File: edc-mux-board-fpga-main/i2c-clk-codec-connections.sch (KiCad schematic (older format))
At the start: 72 parts, among them U57 CDCLVC1108, U58 CDCLVC1108, U59 TCA9555RTWR, U60 TCA9548A, U61 TCA9548A

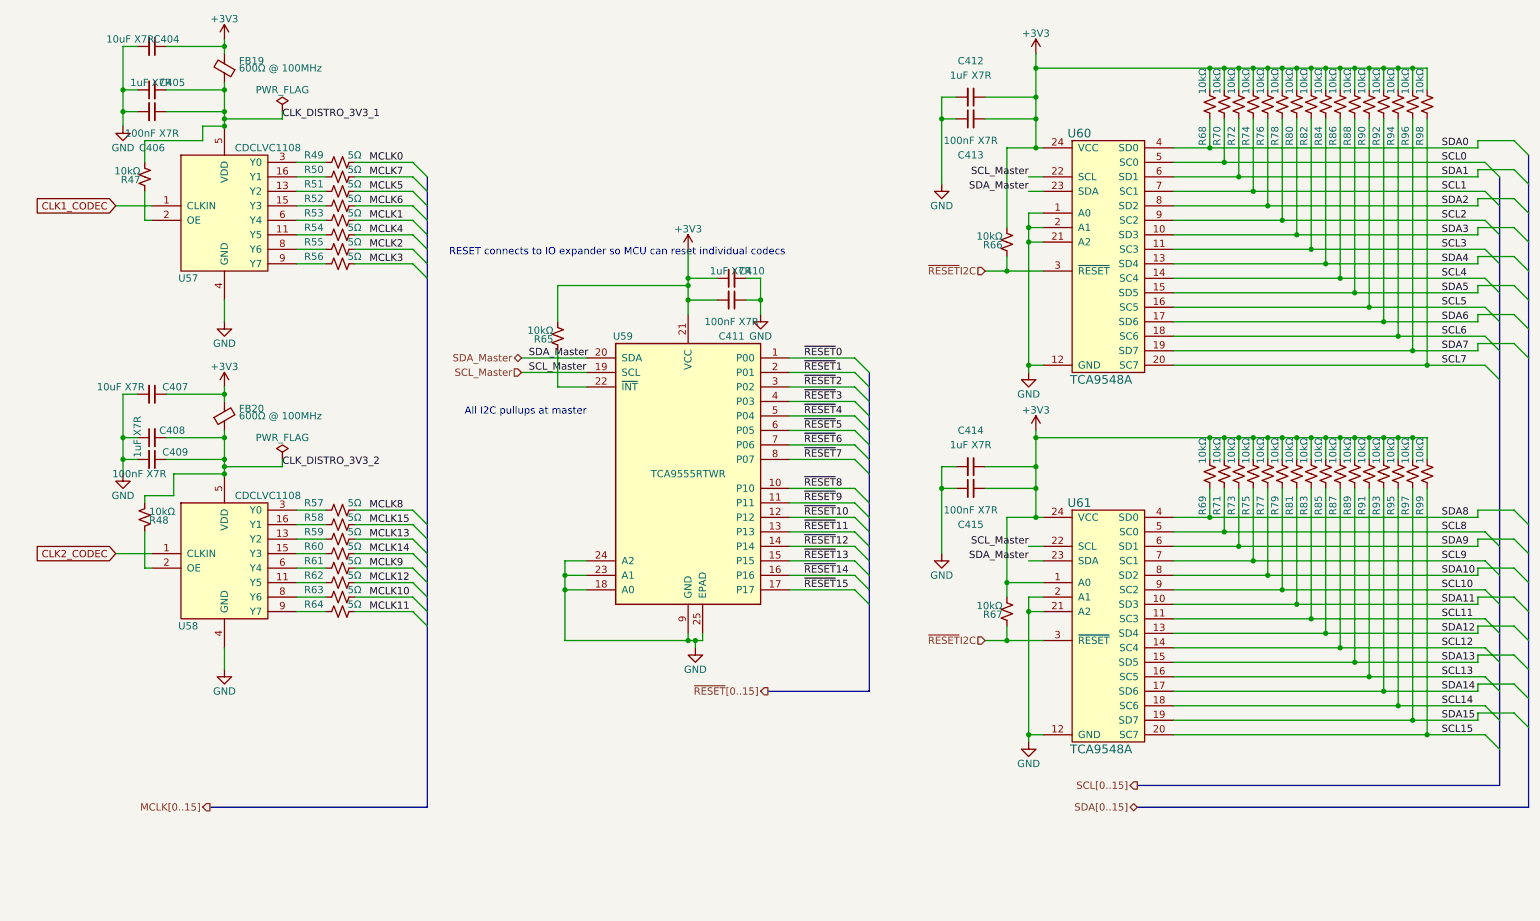
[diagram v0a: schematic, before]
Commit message: removed 8 codecs and support circuitry
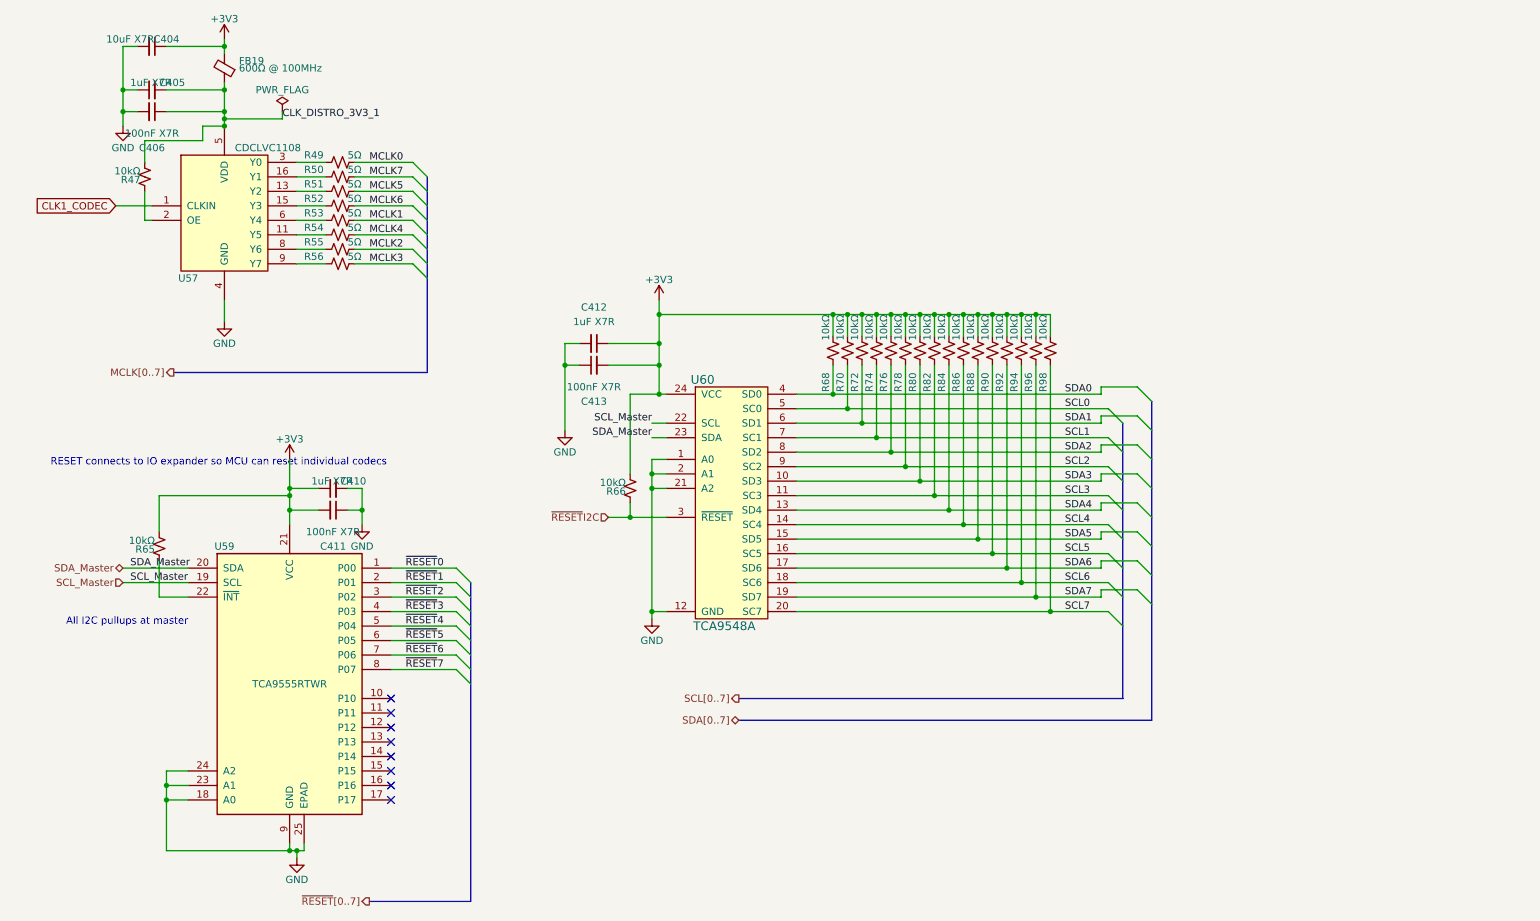
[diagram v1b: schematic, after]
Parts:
- removed C407: 10uF X7R, Capacitor_SMD:C_1206_3216Metric, symbol Device:C_Small
- removed C408, C414: 1uF X7R, Capacitor_SMD:C_0603_1608Metric, symbol Device:C_Small
- removed C409, C415: 100nF X7R, Capacitor_SMD:C_0603_1608Metric, symbol Device:C_Small
- removed FB20: 600Ω @ 100MHz, Inductor_SMD:L_0805_2012Metric, symbol Device:Ferrite_Bead_Small
- removed R48, R67, R69, R71, R73, R75, R77, R79, R81, R83, R85, R87, R89, R91, R93, R95, R97, R99: 10kΩ, Resistor_SMD:R_0402_1005Metric, symbol Device:R_Small_US
- removed R57, R58, R59, R60, R61, R62, R63, R64: 5Ω, Resistor_SMD:R_0402_1005Metric, symbol Device:R_Small_US
- removed U58: CDCLVC1108, Package_SO:TSSOP-16_4.4x5mm_P0.65mm, symbol SW-Texas:CDCLVC1108
- removed U61: TCA9548A, Package_SO:TSSOP-24_4.4x7.8mm_P0.65mm, symbol SW-Texas:TCA9548A
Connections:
- net ~RESET~10: no longer names the net of U59.12 (P12)
- net ~RESET~11: no longer names the net of U59.13 (P13)
- net ~RESET~12: no longer names the net of U59.14 (P14)
- net ~RESET~13: no longer names the net of U59.15 (P15)
- net ~RESET~14: no longer names the net of U59.16 (P16)
- net ~RESET~15: no longer names the net of U59.17 (P17)
- net ~RESET~8: no longer names the net of U59.10 (P10)
- net ~RESET~9: no longer names the net of U59.11 (P11)
- no-connect marks 0 -> 8
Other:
- moved on the sheet: C410, C411, C412, C413, R65, R66, R68, R70, R72, R74, R76, R78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

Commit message: Reannotate main schematic and pcb after expansion transition
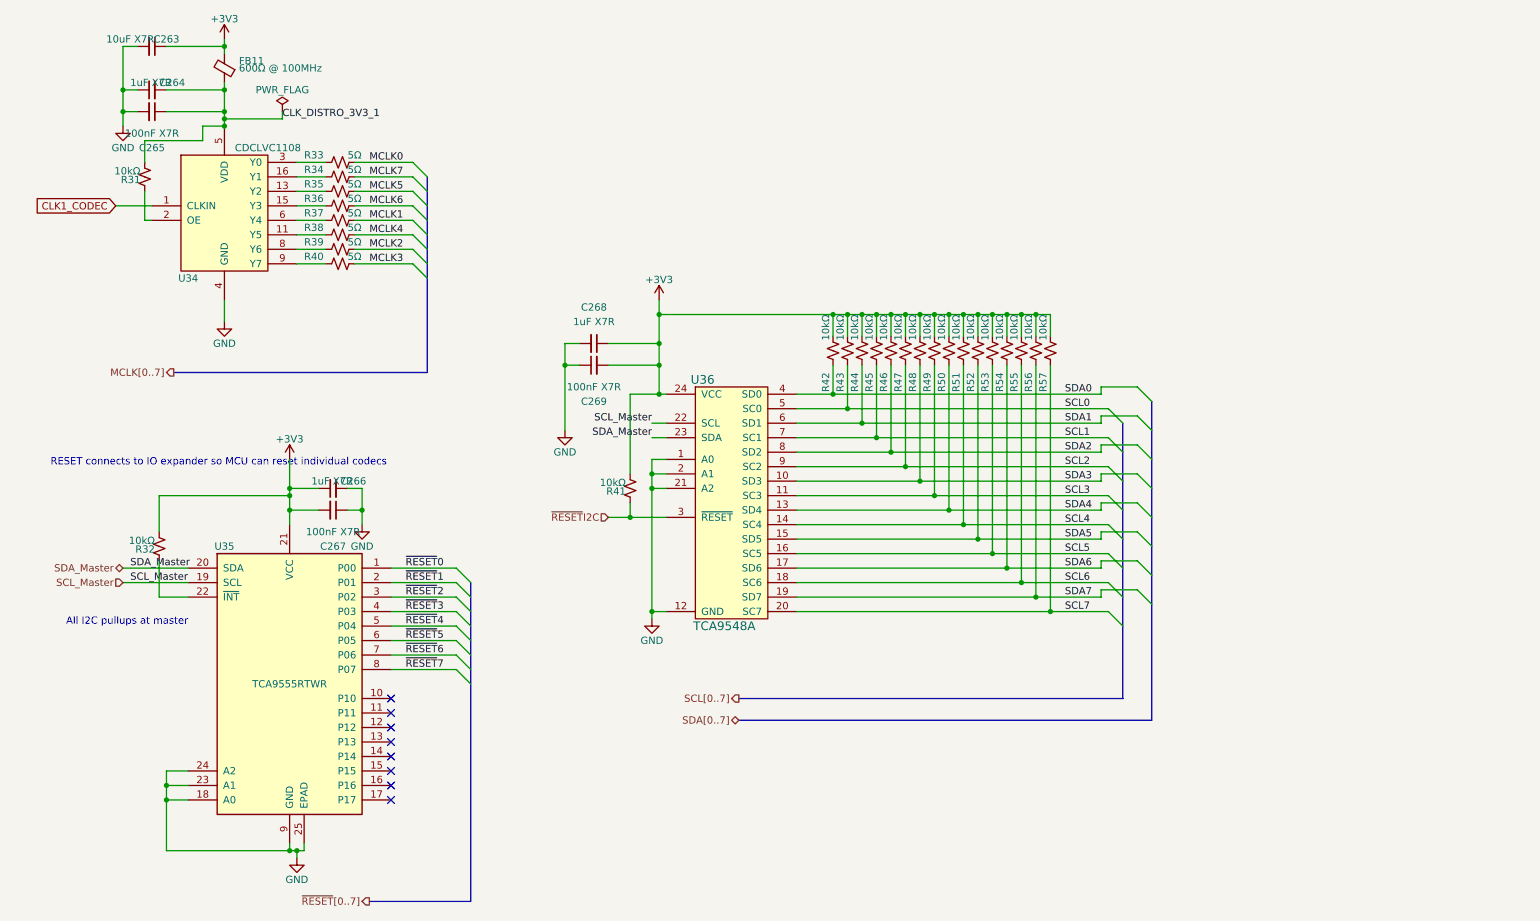
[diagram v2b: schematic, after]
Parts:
- renumbered C404 to C263, C405 to C264, C406 to C265, C410 to C266, C411 to C267, C412 to C268, C413 to C269, FB19 to FB11, R47 to R31, R65 to R32, R49 to R33, R50 to R34, R51 to R35, R52 to R36, R53 to R37, R54 to R38, R55 to R39, R56 to R40, R66 to R41, R68 to R42, R70 to R43, R72 to R44, R74 to R45, R76 to R46, R78 to R47, R80 to R48, R82 to R49, R84 to R50, R86 to R51, R88 to R52, R90 to R53, R92 to R54, R94 to R55, R96 to R56, R98 to R57, U57 to U34, U59 to U35, U60 to U36

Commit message: swapping 100nF capacitors from 0603 to 0402 size
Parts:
- C265, C267, C269: footprint Capacitor_SMD:C_0603_1608Metric -> Capacitor_SMD:C_0402_1005Metric; Characteristics CAP CER 0.1UF 25V X7R 0603 -> CAP CER 0.1UF 25V X7R 0402; Manufacturer Kemet -> AVX; Manufacturers Part Number C0603C104J3RACAUTO -> 04023C104JAT2A; Package ID 0603in/1608mm -> 0402in/1005mm
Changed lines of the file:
@@
 F 0 "C265" V 1200 1350 50  0000 C CNN
 F 1 "100nF X7R" V 1300 1350 50  0000 C CNN
-F 2 "Capacitor_SMD:C_0603_1608Metric" H 1450 1350 50  0001 C CNN
-F 3 "https://content.kemet.com/datasheets/KEM_C1023_X7R_AUTO_SMD.pdf" H 1450 1350 50  0001 C CNN
-F 4 "0603in/1608mm" H -6000 -2400 50  0001 C CNN "Package ID"
-F 5 "Kemet" H 0   0   50  0001 C CNN "Manufacturer"
-F 6 "C0603C104J3RACAUTO" H 0   0   50  0001 C CNN "Manufacturers Part Number"
-F 7 "CAP CER 0.1UF 25V X7R 0603" H 0   0   50  0001 C CNN "Characteristics"
+F 2 "Capacitor_SMD:C_0402_1005Metric" H 1450 1350 50  0001 C CNN
+F 3 "http://datasheets.avx.com/X7RDielectric.pdf" H 1450 1350 50  0001 C CNN
+F 4 "0402in/1005mm" H -6000 -2400 50  0001 C CNN "Package ID"
+F 5 "AVX" H 0   0   50  0001 C CNN "Manufacturer"
+F 6 "04023C104JAT2A" H 0   0   50  0001 C CNN "Manufacturers Part Number"
+F 7 "CAP CER 0.1UF 25V X7R 0402" H 0   0   50  0001 C CNN "Characteristics"
 F 8 "MLCC Capacitor" H 0   0   50  0001 C CNN "Description"
 	1    1450 1350
@@
 F 0 "C267" V 2450 4100 50  0000 C CNN
 F 1 "100nF X7R" V 2550 4100 50  0000 C CNN
-F 2 "Capacitor_SMD:C_0603_1608Metric" H 2700 4100 50  0001 C CNN
-F 3 "https://content.kemet.com/datasheets/KEM_C1023_X7R_AUTO_SMD.pdf" H 2700 4100 50  0001 C CNN
-F 4 "0603in/1608mm" H -4750 350 50  0001 C CNN "Package ID"
-F 5 "Kemet" H -2750 1450 50  0001 C CNN "Manufacturer"
-F 6 "C0603C104J3RACAUTO" H -2750 1450 50  0001 C CNN "Manufacturers Part Number"
-F 7 "CAP CER 0.1UF 25V X7R 0603" H -2750 1450 50  0001 C CNN "Characteristics"
+F 2 "Capacitor_SMD:C_0402_1005Metric" H 2700 4100 50  0001 C CNN
+F 3 "http://datasheets.avx.com/X7RDielectric.pdf" H 2700 4100 50  0001 C CNN
+F 4 "0402in/1005mm" H -4750 350 50  0001 C CNN "Package ID"
+F 5 "AVX" H -2750 1450 50  0001 C CNN "Manufacturer"
+F 6 "04023C104JAT2A" H -2750 1450 50  0001 C CNN "Manufacturers Part Number"
+F 7 "CAP CER 0.1UF 25V X7R 0402" H -2750 1450 50  0001 C CNN "Characteristics"
 F 8 "MLCC Capacitor" H -2750 1450 50  0001 C CNN "Description"
 	1    2700 4100
@@
 F 0 "C269" V 4250 3100 50  0000 C CNN
 F 1 "100nF X7R" V 4350 3100 50  0000 C CNN
-F 2 "Capacitor_SMD:C_0603_1608Metric" H 4500 3100 50  0001 C CNN
-F 3 "https://content.kemet.com/datasheets/KEM_C1023_X7R_AUTO_SMD.pdf" H 4500 3100 50  0001 C CNN
-F 4 "0603in/1608mm" H -2950 -650 50  0001 C CNN "Package ID"
-F 5 "Kemet" H -2600 1700 50  0001 C CNN "Manufacturer"
-F 6 "C0603C104J3RACAUTO" H -2600 1700 50  0001 C CNN "Manufacturers Part Number"
-F 7 "CAP CER 0.1UF 25V X7R 0603" H -2600 1700 50  0001 C CNN "Characteristics"
+F 2 "Capacitor_SMD:C_0402_1005Metric" H 4500 3100 50  0001 C CNN
+F 3 "http://datasheets.avx.com/X7RDielectric.pdf" H 4500 3100 50  0001 C CNN
+F 4 "0402in/1005mm" H -2950 -650 50  0001 C CNN "Package ID"
+F 5 "AVX" H -2600 1700 50  0001 C CNN "Manufacturer"
+F 6 "04023C104JAT2A" H -2600 1700 50  0001 C CNN "Manufacturers Part Number"
+F 7 "CAP CER 0.1UF 25V X7R 0402" H -2600 1700 50  0001 C CNN "Characteristics"
 F 8 "MLCC Capacitor" H -2600 1700 50  0001 C CNN "Description"
 	1    4500 3100
